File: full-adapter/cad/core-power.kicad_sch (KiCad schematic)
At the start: 22 parts, among them U1 RK3568B2

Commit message: bom: use current production core capacitors and retain bias curves
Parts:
- C202, C203, C204, C209, C210, C214, C215, C218, C219: LCSC C45783 -> C602037; MPN CL21A226MAQNNNE -> CL21A226MAYNNNE
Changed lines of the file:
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@@
 (property "Description" "Unpolarized capacitor" (at 195.58 57.14999999999999 0) (effects (font (size 1.27 1.27)) (justify left)) (hide yes))
 (property "Manufacturer" "Samsung Electro-Mechanics" (at 195.58 59.69 0) (effects (font (size 1.27 1.27)) (justify left)) (hide yes))
-(property "MPN" "CL21A226MAQNNNE" (at 195.58 62.23 0) (effects (font (size 1.27 1.27)) (justify left)) (hide yes))
-(property "LCSC" "C45783" (at 195.58 64.77 0) (effects (font (size 1.27 1.27)) (justify left)) (hide yes))
+(property "MPN" "CL21A226MAYNNNE" (at 195.58 62.23 0) (effects (font (size 1.27 1.27)) (justify left)) (hide yes))
+(property "LCSC" "C602037" (at 195.58 64.77 0) (effects (font (size 1.27 1.27)) (justify left)) (hide yes))
 (pin "1")
 (pin "2")(instances (project "full-adapter" (path "/fda20879-fa66-56c0-be14-de2506349b46/2cb54c12-b544-5fde-96a4-0c9983539cc3" (reference "C202") (unit 1)))))
@@
 (property "Description" "Unpolarized capacitor" (at 226.06 57.14999999999999 0) (effects (font (size 1.27 1.27)) (justify left)) (hide yes))
 (property "Manufacturer" "Samsung Electro-Mechanics" (at 226.06 59.69 0) (effects (font (size 1.27 1.27)) (justify left)) (hide yes))
-(property "MPN" "CL21A226MAQNNNE" (at 226.06 62.23 0) (effects (font (size 1.27 1.27)) (justify left)) (hide yes))
-(property "LCSC" "C45783" (at 226.06 64.77 0) (effects (font (size 1.27 1.27)) (justify left)) (hide yes))
+(property "MPN" "CL21A226MAYNNNE" (at 226.06 62.23 0) (effects (font (size 1.27 1.27)) (justify left)) (hide yes))
+(property "LCSC" "C602037" (at 226.06 64.77 0) (effects (font (size 1.27 1.27)) (justify left)) (hide yes))
 (pin "1")
 (pin "2")(instances (project "full-adapter" (path "/fda20879-fa66-56c0-be14-de2506349b46/2cb54c12-b544-5fde-96a4-0c9983539cc3" (reference "C203") (unit 1)))))
@@
 (property "Description" "Unpolarized capacitor" (at 256.54 57.14999999999999 0) (effects (font (size 1.27 1.27)) (justify left)) (hide yes))
 (property "Manufacturer" "Samsung Electro-Mechanics" (at 256.54 59.69 0) (effects (font (size 1.27 1.27)) (justify left)) (hide yes))
-(property "MPN" "CL21A226MAQNNNE" (at 256.54 62.23 0) (effects (font (size 1.27 1.27)) (justify left)) (hide yes))
-(property "LCSC" "C45783" (at 256.54 64.77 0) (effects (font (size 1.27 1.27)) (justify left)) (hide yes))
+(property "MPN" "CL21A226MAYNNNE" (at 256.54 62.23 0) (effects (font (size 1.27 1.27)) (justify left)) (hide yes))
+(property "LCSC" "C602037" (at 256.54 64.77 0) (effects (font (size 1.27 1.27)) (justify left)) (hide yes))
 (pin "1")
 (pin "2")(instances (project "full-adapter" (path "/fda20879-fa66-56c0-be14-de2506349b46/2cb54c12-b544-5fde-96a4-0c9983539cc3" (reference "C204") (unit 1)))))
@@
 (property "Description" "Unpolarized capacitor" (at 256.54 85.09 0) (effects (font (size 1.27 1.27)) (justify left)) (hide yes))
 (property "Manufacturer" "Samsung Electro-Mechanics" (at 256.54 87.63000000000001 0) (effects (font (size 1.27 1.27)) (justify left)) (hide yes))
-(property "MPN" "CL21A226MAQNNNE" (at 256.54 90.17 0) (effects (font (size 1.27 1.27)) (justify left)) (hide yes))
-(property "LCSC" "C45783" (at 256.54 92.71000000000001 0) (effects (font (size 1.27 1.27)) (justify left)) (hide yes))
+(property "MPN" "CL21A226MAYNNNE" (at 256.54 90.17 0) (effects (font (size 1.27 1.27)) (justify left)) (hide yes))
+(property "LCSC" "C602037" (at 256.54 92.71000000000001 0) (effects (font (size 1.27 1.27)) (justify left)) (hide yes))
 (pin "1")
 (pin "2")(instances (project "full-adapter" (path "/fda20879-fa66-56c0-be14-de2506349b46/2cb54c12-b544-5fde-96a4-0c9983539cc3" (reference "C209") (unit 1)))))
@@
 (property "Description" "Unpolarized capacitor" (at 287.02000000000004 85.09 0) (effects (font (size 1.27 1.27)) (justify left)) (hide yes))
 (property "Manufacturer" "Samsung Electro-Mechanics" (at 287.02000000000004 87.63000000000001 0) (effects (font (size 1.27 1.27)) (justify left)) (hide yes))
-(property "MPN" "CL21A226MAQNNNE" (at 287.02000000000004 90.17 0) (effects (font (size 1.27 1.27)) (justify left)) (hide yes))
-(property "LCSC" "C45783" (at 287.02000000000004 92.71000000000001 0) (effects (font (size 1.27 1.27)) (justify left)) (hide yes))
+(property "MPN" "CL21A226MAYNNNE" (at 287.02000000000004 90.17 0) (effects (font (size 1.27 1.27)) (justify left)) (hide yes))
+(property "LCSC" "C602037" (at 287.02000000000004 92.71000000000001 0) (effects (font (size 1.27 1.27)) (justify left)) (hide yes))
 (pin "1")
 (pin "2")(instances (project "full-adapter" (path "/fda20879-fa66-56c0-be14-de2506349b46/2cb54c12-b544-5fde-96a4-0c9983539cc3" (reference "C210") (unit 1)))))
@@
 (property "Description" "Unpolarized capacitor" (at 195.58 113.03 0) (effects (font (size 1.27 1.27)) (justify left)) (hide yes))
 (property "Manufacturer" "Samsung Electro-Mechanics" (at 195.58 115.57000000000001 0) (effects (font (size 1.27 1.27)) (justify left)) (hide yes))
-(property "MPN" "CL21A226MAQNNNE" (at 195.58 118.11 0) (effects (font (size 1.27 1.27)) (justify left)) (hide yes))
-(property "LCSC" "C45783" (at 195.58 120.65 0) (effects (font (size 1.27 1.27)) (justify left)) (hide yes))
+(property "MPN" "CL21A226MAYNNNE" (at 195.58 118.11 0) (effects (font (size 1.27 1.27)) (justify left)) (hide yes))
+(property "LCSC" "C602037" (at 195.58 120.65 0) (effects (font (size 1.27 1.27)) (justify left)) (hide yes))
 (pin "1")
 (pin "2")(instances (project "full-adapter" (path "/fda20879-fa66-56c0-be14-de2506349b46/2cb54c12-b544-5fde-96a4-0c9983539cc3" (reference "C214") (unit 1)))))
@@
 (property "Description" "Unpolarized capacitor" (at 226.06 113.03 0) (effects (font (size 1.27 1.27)) (justify left)) (hide yes))
 (property "Manufacturer" "Samsung Electro-Mechanics" (at 226.06 115.57000000000001 0) (effects (font (size 1.27 1.27)) (justify left)) (hide yes))
-(property "MPN" "CL21A226MAQNNNE" (at 226.06 118.11 0) (effects (font (size 1.27 1.27)) (justify left)) (hide yes))
-(property "LCSC" "C45783" (at 226.06 120.65 0) (effects (font (size 1.27 1.27)) (justify left)) (hide yes))
+(property "MPN" "CL21A226MAYNNNE" (at 226.06 118.11 0) (effects (font (size 1.27 1.27)) (justify left)) (hide yes))
+(property "LCSC" "C602037" (at 226.06 120.65 0) (effects (font (size 1.27 1.27)) (justify left)) (hide yes))
 (pin "1")
 (pin "2")(instances (project "full-adapter" (path "/fda20879-fa66-56c0-be14-de2506349b46/2cb54c12-b544-5fde-96a4-0c9983539cc3" (reference "C215") (unit 1)))))
@@
 (property "Description" "Unpolarized capacitor" (at 165.1 140.97 0) (effects (font (size 1.27 1.27)) (justify left)) (hide yes))
 (property "Manufacturer" "Samsung Electro-Mechanics" (at 165.1 143.51 0) (effects (font (size 1.27 1.27)) (justify left)) (hide yes))
-(property "MPN" "CL21A226MAQNNNE" (at 165.1 146.05 0) (effects (font (size 1.27 1.27)) (justify left)) (hide yes))
-(property "LCSC" "C45783" (at 165.1 148.59 0) (effects (font (size 1.27 1.27)) (justify left)) (hide yes))
+(property "MPN" "CL21A226MAYNNNE" (at 165.1 146.05 0) (effects (font (size 1.27 1.27)) (justify left)) (hide yes))
+(property "LCSC" "C602037" (at 165.1 148.59 0) (effects (font (size 1.27 1.27)) (justify left)) (hide yes))
 (pin "1")
 (pin "2")(instances (project "full-adapter" (path "/fda20879-fa66-56c0-be14-de2506349b46/2cb54c12-b544-5fde-96a4-0c9983539cc3" (reference "C218") (unit 1)))))
@@
 (property "Description" "Unpolarized capacitor" (at 195.58 140.97 0) (effects (font (size 1.27 1.27)) (justify left)) (hide yes))
 (property "Manufacturer" "Samsung Electro-Mechanics" (at 195.58 143.51 0) (effects (font (size 1.27 1.27)) (justify left)) (hide yes))
-(property "MPN" "CL21A226MAQNNNE" (at 195.58 146.05 0) (effects (font (size 1.27 1.27)) (justify left)) (hide yes))
-(property "LCSC" "C45783" (at 195.58 148.59 0) (effects (font (size 1.27 1.27)) (justify left)) (hide yes))
+(property "MPN" "CL21A226MAYNNNE" (at 195.58 146.05 0) (effects (font (size 1.27 1.27)) (justify left)) (hide yes))
+(property "LCSC" "C602037" (at 195.58 148.59 0) (effects (font (size 1.27 1.27)) (justify left)) (hide yes))
 (pin "1")
 (pin "2")(instances (project "full-adapter" (path "/fda20879-fa66-56c0-be14-de2506349b46/2cb54c12-b544-5fde-96a4-0c9983539cc3" (reference "C219") (unit 1)))))

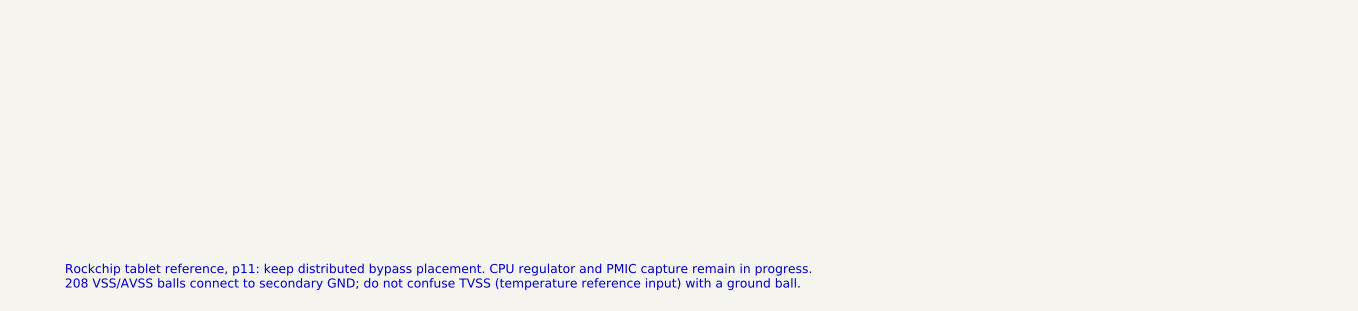
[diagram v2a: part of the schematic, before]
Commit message: Capture processor 24 MHz oscillator and TVSS reference
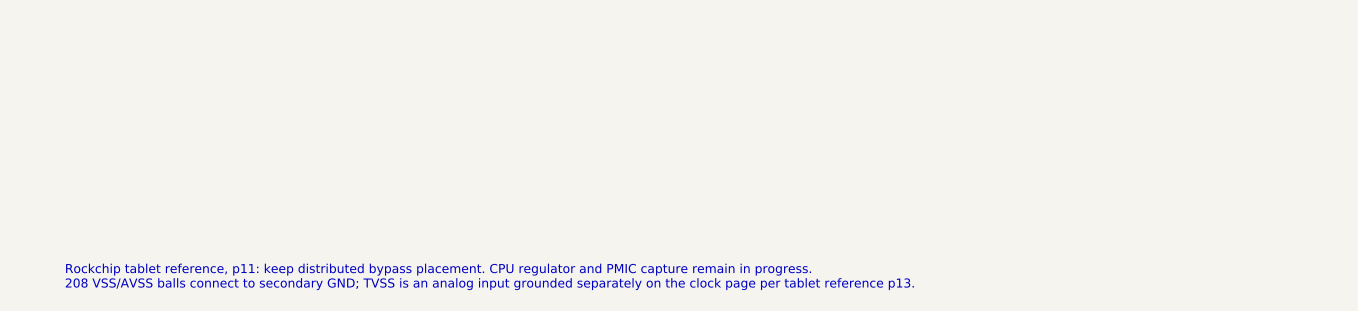
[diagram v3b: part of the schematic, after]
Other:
- note added: "Rockchip tablet reference, p11: keep distributed bypass placement. CPU regulator and PMIC capture remain in progress. 208 VSS/AVSS balls connect to secondary GND; TVSS is an analog input grounded separately on the clock page per tablet reference p13."
- note removed: "Rockchip tablet reference, p11: keep distributed bypass placement. CPU regulator and PMIC capture remain in progress. 208 VSS/AVSS balls connect to secondary GND; do not confuse TVSS (temperature reference input) with a ground ball."
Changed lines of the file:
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@@
 (property "Description" "Power symbol creates a global label with name \"GND\" , ground" (at 388.62 251.46 0) (effects (font (size 1.27 1.27))) (hide yes))
 (pin "1")(instances (project "full-adapter" (path "/fda20879-fa66-56c0-be14-de2506349b46/2cb54c12-b544-5fde-96a4-0c9983539cc3" (reference "#PWRcorepower020") (unit 1)))))
-(text "Rockchip tablet reference, p11: keep distributed bypass placement. CPU regulator and PMIC capture remain in progress.\n208 VSS/AVSS balls connect to secondary GND; do not confuse TVSS (temperature reference input) with a ground ball." (at 15.24 281.94 0) (effects (font (size 1.0 1.0)) (justify left top)))
+(text "Rockchip tablet reference, p11: keep distributed bypass placement. CPU regulator and PMIC capture remain in progress.\n208 VSS/AVSS balls connect to secondary GND; TVSS is an analog input grounded separately on the clock page per tablet reference p13." (at 15.24 281.94 0) (effects (font (size 1.0 1.0)) (justify left top)))
 )
